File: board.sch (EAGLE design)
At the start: 17 parts, among them J2 632723300011, Q1 16Mhz, U1 MICROCHIP_TECHNOLOGY_MIC5219-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

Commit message: Add reset switch; Minor cleanup
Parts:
- added R6: 10k, rcl:R-EU_R0805
- added S1: (no value), SparkFun-Switches:MOMENTARY-SWITCH-SPST-2-SMD-4.6X2.8MM
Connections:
- new net N$5: R6.2, S1.3, U$1./RESET
- new net N$6: U$1.UVCC
- net GND: now also S1.1
- net VBUS: now also U$1.VBUS
- net VCC: now also R6.1
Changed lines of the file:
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@@
 <part name="C7" library="rcl" library_urn="urn:adsk.eagle:library:334" deviceset="CPOL-EU" device="SMCB" package3d_urn="urn:adsk.eagle:package:25920/5" value="10uF"/>
 <part name="P+2" library="supply1" library_urn="urn:adsk.eagle:library:371" deviceset="VCC" device=""/>
+<part name="P+3" library="supply1" library_urn="urn:adsk.eagle:library:371" deviceset="VCC" device=""/>
+<part name="R6" library="rcl" library_urn="urn:adsk.eagle:library:334" deviceset="R-EU_" device="R0805" package3d_urn="urn:adsk.eagle:package:23553/2" value="10k"/>
+<part name="S1" library="SparkFun-Switches" library_urn="urn:adsk.eagle:library:535" deviceset="MOMENTARY-SWITCH-SPST-2" device="-SMD-4.6X2.8MM" package3d_urn="urn:adsk.eagle:package:40176/1"/>
+<part name="GND10" library="supply1" library_urn="urn:adsk.eagle:library:371" deviceset="GND" device=""/>
 </parts>
 <sheets>
@@
 <segment>
 <pinref part="U1" gate="G$0" pin="IN"/>
-<wire x1="30.48" y1="99.06" x2="22.86" y2="99.06" width="0.1524" layer="91"/>
-<wire x1="22.86" y1="99.06" x2="22.86" y2="83.82" width="0.1524" layer="91"/>
+<wire x1="30.48" y1="99.06" x2="27.94" y2="99.06" width="0.1524" layer="91"/>
+<wire x1="27.94" y1="99.06" x2="27.94" y2="83.82" width="0.1524" layer="91"/>
 <pinref part="U1" gate="G$0" pin="EN"/>
-<wire x1="22.86" y1="83.82" x2="30.48" y2="83.82" width="0.1524" layer="91"/>
-<junction x="22.86" y="99.06"/>
-<label x="7.62" y="99.06" size="1.778" layer="95" rot="R180"/>
-<wire x1="22.86" y1="99.06" x2="15.24" y2="99.06" width="0.1524" layer="91"/>
+<wire x1="27.94" y1="83.82" x2="30.48" y2="83.82" width="0.1524" layer="91"/>
+<junction x="27.94" y="99.06"/>
+<label x="27.94" y="104.14" size="1.778" layer="95" rot="R90" xref="yes"/>
 <pinref part="C7" gate="G$1" pin="+"/>
-<wire x1="15.24" y1="99.06" x2="7.62" y2="99.06" width="0.1524" layer="91"/>
+<wire x1="27.94" y1="99.06" x2="15.24" y2="99.06" width="0.1524" layer="91"/>
 <wire x1="15.24" y1="99.06" x2="15.24" y2="96.52" width="0.1524" layer="91"/>
 <junction x="15.24" y="99.06"/>
+<label x="15.24" y="104.14" size="1.778" layer="95" rot="R90"/>
+<wire x1="15.24" y1="99.06" x2="15.24" y2="104.14" width="0.1524" layer="91"/>
+<wire x1="27.94" y1="104.14" x2="27.94" y2="99.06" width="0.1524" layer="91"/>
+<junction x="27.94" y="99.06"/>
 </segment>
 </net>
@@
 <attribute name="VALUE" x="22.86" y="2.54" size="1.778" layer="96"/>
 </instance>
+<instance part="P+3" gate="VCC" x="2.54" y="83.82" smashed="yes" rot="R90">
+<attribute name="VALUE" x="2.54" y="86.36" size="1.778" layer="96" rot="R180"/>
+</instance>
+<instance part="R6" gate="G$1" x="15.24" y="83.82" smashed="yes">
+<attribute name="NAME" x="11.43" y="85.3186" size="1.778" layer="95"/>
+<attribute name="VALUE" x="11.43" y="80.518" size="1.778" layer="96"/>
+</instance>
+<instance part="S1" gate="G$1" x="15.24" y="91.44" smashed="yes">
+<attribute name="NAME" x="15.24" y="96.266" size="1.778" layer="95" font="vector" align="bottom-center"/>
+<attribute name="VALUE" x="15.24" y="88.646" size="1.778" layer="96" font="vector" align="top-center"/>
+</instance>
+<instance part="GND10" gate="1" x="2.54" y="91.44" smashed="yes" rot="R270">
+<attribute name="VALUE" x="0" y="93.98" size="1.778" layer="96" rot="R270"/>
+</instance>
 </instances>
 <busses>
@@
 <junction x="25.4" y="15.24"/>
 </segment>
+<segment>
+<pinref part="GND10" gate="1" pin="GND"/>
+<pinref part="S1" gate="G$1" pin="1"/>
+<wire x1="5.08" y1="91.44" x2="10.16" y2="91.44" width="0.1524" layer="91"/>
+</segment>
 </net>
 <net name="N$7" class="0">
@@
 </segment>
 </net>
+<net name="VBUS" class="0">
+<segment>
+<pinref part="U$1" gate="G$1" pin="VBUS"/>
+<wire x1="25.4" y1="78.74" x2="20.32" y2="78.74" width="0.1524" layer="91"/>
+<label x="20.32" y="78.74" size="1.27" layer="95" rot="R180" xref="yes"/>
+</segment>
+</net>
+<net name="N$6" class="0">
+<segment>
+<pinref part="U$1" gate="G$1" pin="UVCC"/>
+<wire x1="25.4" y1="66.04" x2="20.32" y2="66.04" width="0.1524" layer="91"/>
+</segment>
+</net>
+<net name="VCC" class="0">
+<segment>
+<pinref part="P+3" gate="VCC" pin="VCC"/>
+<pinref part="R6" gate="G$1" pin="1"/>
+<wire x1="5.08" y1="83.82" x2="10.16" y2="83.82" width="0.1524" layer="91"/>
+</segment>
+</net>
+<net name="N$5" class="0">
+<segment>
+<pinref part="R6" gate="G$1" pin="2"/>
+<pinref part="U$1" gate="G$1" pin="/RESET"/>
+<wire x1="20.32" y1="83.82" x2="25.4" y2="83.82" width="0.1524" layer="91"/>
+<wire x1="25.4" y1="83.82" x2="25.4" y2="91.44" width="0.1524" layer="91"/>
+<junction x="25.4" y="83.82"/>
+<pinref part="S1" gate="G$1" pin="3"/>
+<wire x1="20.32" y1="91.44" x2="25.4" y2="91.44" width="0.1524" layer="91"/>
+</segment>
+</net>

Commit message: Add connections for AtMega32u4
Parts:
- added C10, C8: 1uF, rcl:C-EUC0805
- added C9: 100nF, rcl:C-EUC0805
- added L1: MH2029-300Y, rcl:L-EUL2012C
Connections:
- new net N$8: C9.2, U$1.AREF
- new net N$9: C10.2, L1.1, U$1.AVCC, U$1.AVCC1
- net D+: now also U$1.D+
- net D-: now also U$1.D-
- net GND: now also C10.1, C8.1, C9.1, U$1.UGND
- net N$6: now also C8.2, U$1.UCAP; no longer U$1.UVCC
- net VCC: now also L1.2, U$1.UVCC, U$1.VCC, U$1.VCC1
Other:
- moved on the sheet: C1, C2, Q1

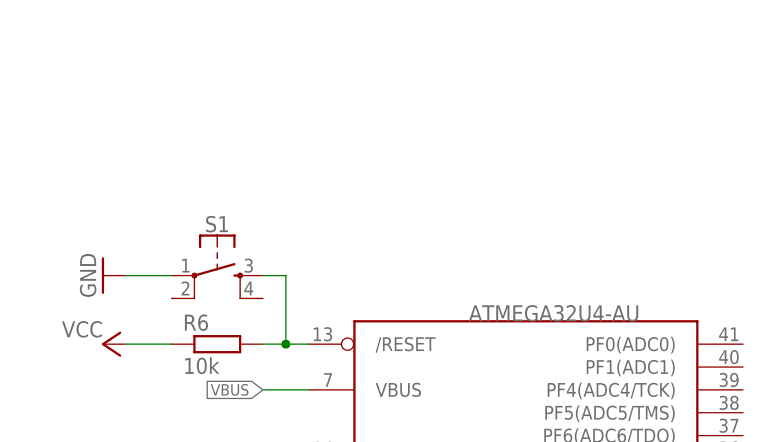
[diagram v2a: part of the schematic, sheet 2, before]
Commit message: Add ISP-6 Header
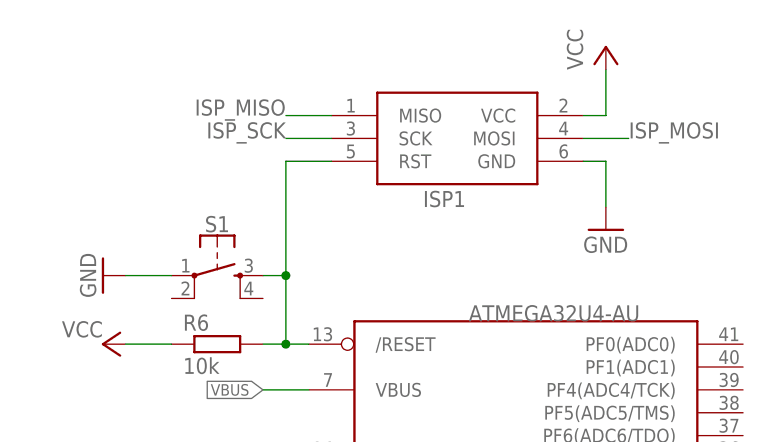
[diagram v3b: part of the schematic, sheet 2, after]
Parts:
- added ISP1: AVRISP-6, adafruit:AVRISP-6
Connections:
- new net ISP_MISO: ISP1.MISO
- new net ISP_MOSI: ISP1.MOSI
- new net ISP_SCK: ISP1.SCK
- net GND: now also ISP1.GND
- net N$5: now also ISP1.RST
- net VCC: now also ISP1.VCC
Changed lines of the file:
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@@
 <part name="GND13" library="supply1" library_urn="urn:adsk.eagle:library:371" deviceset="GND" device=""/>
 <part name="GND14" library="supply1" library_urn="urn:adsk.eagle:library:371" deviceset="GND" device=""/>
+<part name="ISP1" library="adafruit" library_urn="urn:adsk.eagle:library:420" deviceset="AVRISP" device="-6" package3d_urn="urn:adsk.eagle:package:6240744/1"/>
+<part name="P+5" library="supply1" library_urn="urn:adsk.eagle:library:371" deviceset="VCC" device=""/>
+<part name="GND15" library="supply1" library_urn="urn:adsk.eagle:library:371" deviceset="GND" device=""/>
 </parts>
 <sheets>
@@
 <instance part="GND14" gate="1" x="-5.08" y="48.26" smashed="yes" rot="R270">
 <attribute name="VALUE" x="-7.62" y="50.8" size="1.778" layer="96" rot="R270"/>
+</instance>
+<instance part="ISP1" gate="G$1" x="40.64" y="106.68" smashed="yes">
+<attribute name="NAME" x="38.1" y="99.06" size="1.778" layer="95"/>
+</instance>
+<instance part="P+5" gate="VCC" x="58.42" y="116.84" smashed="yes">
+<attribute name="VALUE" x="55.88" y="114.3" size="1.778" layer="96" rot="R90"/>
+</instance>
+<instance part="GND15" gate="1" x="58.42" y="96.52" smashed="yes">
+<attribute name="VALUE" x="55.88" y="93.98" size="1.778" layer="96"/>
 </instance>
 </instances>
@@
 <wire x1="-2.54" y1="60.96" x2="2.54" y2="60.96" width="0.1524" layer="91"/>
 </segment>
+<segment>
+<pinref part="ISP1" gate="G$1" pin="GND"/>
+<wire x1="55.88" y1="104.14" x2="58.42" y2="104.14" width="0.1524" layer="91"/>
+<wire x1="58.42" y1="104.14" x2="58.42" y2="99.06" width="0.1524" layer="91"/>
+<pinref part="GND15" gate="1" pin="GND"/>
+</segment>
 </net>
 <net name="N$7" class="0">
@@
 <junction x="15.24" y="71.12"/>
 </segment>
+<segment>
+<pinref part="P+5" gate="VCC" pin="VCC"/>
+<wire x1="58.42" y1="114.3" x2="58.42" y2="109.22" width="0.1524" layer="91"/>
+<pinref part="ISP1" gate="G$1" pin="VCC"/>
+<wire x1="58.42" y1="109.22" x2="55.88" y2="109.22" width="0.1524" layer="91"/>
+</segment>
 </net>
 <net name="N$5" class="0">
@@
 <wire x1="22.86" y1="83.82" x2="22.86" y2="91.44" width="0.1524" layer="91"/>
 <junction x="22.86" y="83.82"/>
+<pinref part="ISP1" gate="G$1" pin="RST"/>
+<wire x1="27.94" y1="104.14" x2="22.86" y2="104.14" width="0.1524" layer="91"/>
+<wire x1="22.86" y1="104.14" x2="22.86" y2="91.44" width="0.1524" layer="91"/>
+<junction x="22.86" y="91.44"/>
 </segment>
 </net>
@@
 </segment>
 </net>
+<net name="ISP_SCK" class="0">
+<segment>
+<pinref part="ISP1" gate="G$1" pin="SCK"/>
+<wire x1="27.94" y1="106.68" x2="22.86" y2="106.68" width="0.1524" layer="91"/>
+<label x="22.86" y="106.68" size="1.778" layer="95" rot="R180" align="top-left"/>
+</segment>
+</net>
+<net name="ISP_MISO" class="0">
+<segment>
+<pinref part="ISP1" gate="G$1" pin="MISO"/>
+<wire x1="27.94" y1="109.22" x2="22.86" y2="109.22" width="0.1524" layer="91"/>
+<label x="22.86" y="109.22" size="1.778" layer="95" rot="R180" align="top-left"/>
+</segment>
+</net>
+<net name="ISP_MOSI" class="0">
+<segment>
+<pinref part="ISP1" gate="G$1" pin="MOSI"/>
+<wire x1="55.88" y1="106.68" x2="60.96" y2="106.68" width="0.1524" layer="91"/>
+<label x="60.96" y="106.68" size="1.778" layer="95"/>
+</segment>
+</net>

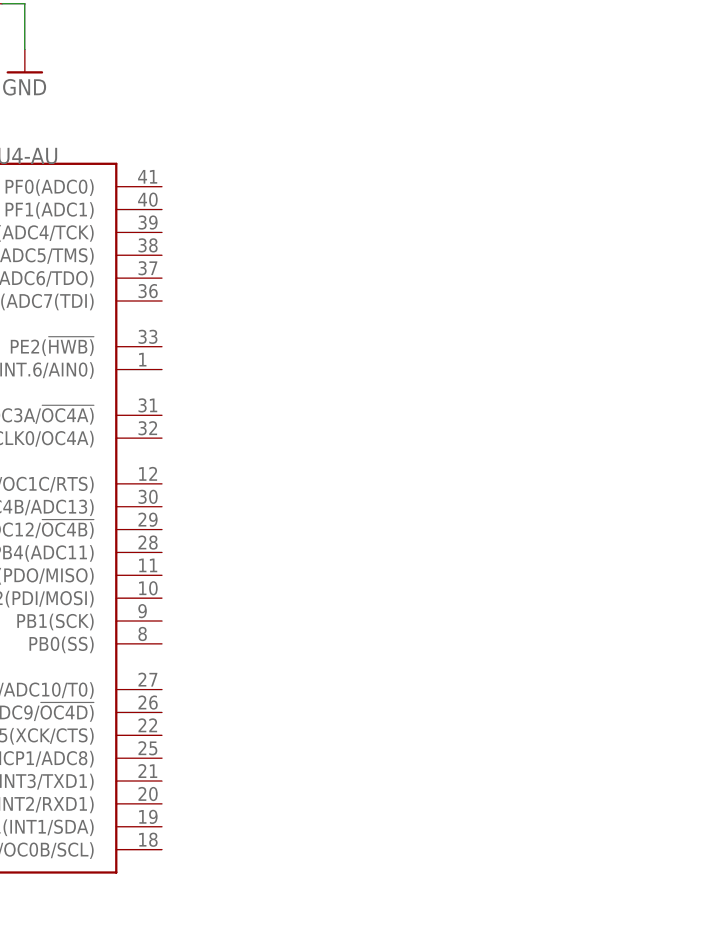
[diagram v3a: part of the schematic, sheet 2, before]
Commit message: Add Analog and Digital IO header
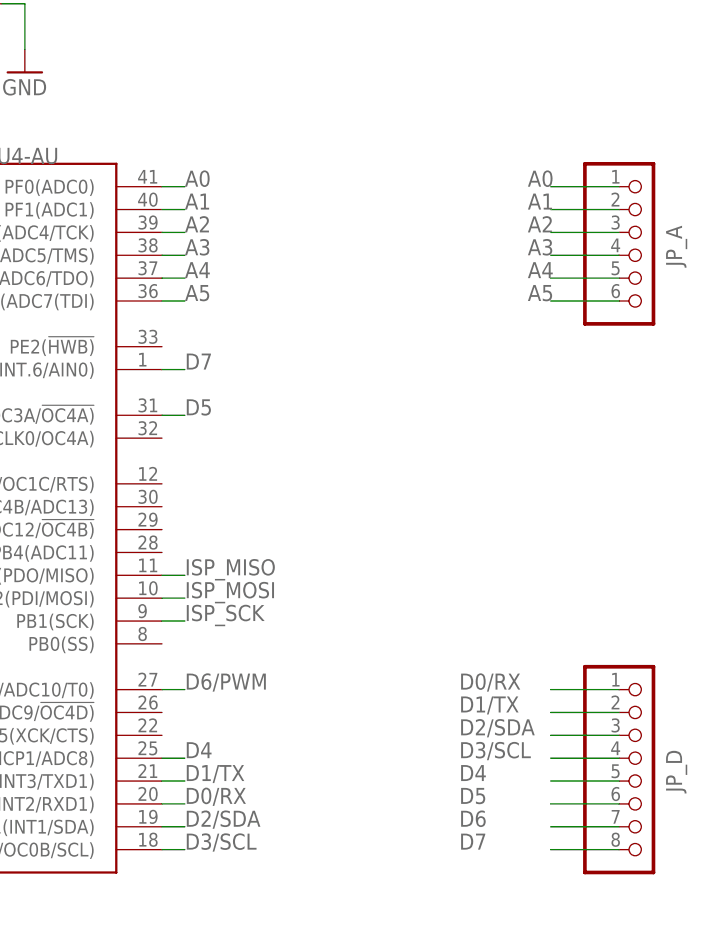
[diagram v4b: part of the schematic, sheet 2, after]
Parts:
- added JP_A: (no value), pinhead:PINHD-1X6
- added JP_D: (no value), pinhead:PINHD-1X8
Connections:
- new net A0: JP_A.1, U$1.PF0(ADC0)
- new net A1: JP_A.2, U$1.PF1(ADC1)
- new net A2: JP_A.3, U$1.PF4(ADC4/TCK)
- new net A3: JP_A.4, U$1.PF5(ADC5/TMS)
- new net A4: JP_A.5, U$1.PF6(ADC6/TDO)
- new net A5: JP_A.6, U$1.PF7(ADC7(TDI)
- new net D0/RX: JP_D.1, U$1.PD2(INT2/RXD1)
- new net D1/TX: JP_D.2, U$1.PD3(INT3/TXD1)
- new net D2/SDA: JP_D.3, U$1.PD1(INT1/SDA)
- new net D3/SCL: JP_D.4, U$1.PD0(INT0/OC0B/SCL)
- new net D4: JP_D.5, U$1.PD4(ICP1/ADC8)
- new net D5: JP_D.6, U$1.PC6(OC3A/!OC4A)
- new net D6: JP_D.7
- new net D6/PWM: U$1.PD7(OC4D/ADC10/T0)
- new net D7: JP_D.8, U$1.PE6(INT.6/AIN0)
- net ISP_MISO: now also U$1.PB3(PDO/MISO)
- net ISP_MOSI: now also U$1.PB2(PDI/MOSI)
- net ISP_SCK: now also U$1.PB1(SCK)
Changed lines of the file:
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@@
 <part name="P+5" library="supply1" library_urn="urn:adsk.eagle:library:371" deviceset="VCC" device=""/>
 <part name="GND15" library="supply1" library_urn="urn:adsk.eagle:library:371" deviceset="GND" device=""/>
+<part name="JP_A" library="pinhead" library_urn="urn:adsk.eagle:library:325" deviceset="PINHD-1X6" device="" package3d_urn="urn:adsk.eagle:package:22472/2"/>
+<part name="JP_D" library="pinhead" library_urn="urn:adsk.eagle:library:325" deviceset="PINHD-1X8" device="" package3d_urn="urn:adsk.eagle:package:22409/2"/>
 </parts>
 <sheets>
@@
 <instance part="GND15" gate="1" x="58.42" y="96.52" smashed="yes">
 <attribute name="VALUE" x="55.88" y="93.98" size="1.778" layer="96"/>
+</instance>
+<instance part="JP_A" gate="A" x="127" y="76.2" smashed="yes">
+<attribute name="NAME" x="131.445" y="74.93" size="1.778" layer="95" rot="R90"/>
+<attribute name="VALUE" x="120.65" y="66.04" size="1.778" layer="96"/>
+</instance>
+<instance part="JP_D" gate="A" x="127" y="17.78" smashed="yes">
+<attribute name="NAME" x="131.445" y="16.51" size="1.778" layer="95" rot="R90"/>
+<attribute name="VALUE" x="120.65" y="5.08" size="1.778" layer="96"/>
 </instance>
 </instances>
@@
 <label x="22.86" y="106.68" size="1.778" layer="95" rot="R180" align="top-left"/>
 </segment>
+<segment>
+<pinref part="U$1" gate="G$1" pin="PB1(SCK)"/>
+<wire x1="73.66" y1="35.56" x2="76.2" y2="35.56" width="0.1524" layer="91"/>
+<label x="76.2" y="35.56" size="1.778" layer="95"/>
+</segment>
 </net>
 <net name="ISP_MISO" class="0">
@@
 <label x="22.86" y="109.22" size="1.778" layer="95" rot="R180" align="top-left"/>
 </segment>
+<segment>
+<pinref part="U$1" gate="G$1" pin="PB3(PDO/MISO)"/>
+<wire x1="73.66" y1="40.64" x2="76.2" y2="40.64" width="0.1524" layer="91"/>
+<label x="76.2" y="40.64" size="1.778" layer="95"/>
+</segment>
 </net>
 <net name="ISP_MOSI" class="0">
@@
 <label x="60.96" y="106.68" size="1.778" layer="95"/>
 </segment>
-</net>
+<segment>
+<pinref part="U$1" gate="G$1" pin="PB2(PDI/MOSI)"/>
+<wire x1="73.66" y1="38.1" x2="76.2" y2="38.1" width="0.1524" layer="91"/>
+<label x="76.2" y="38.1" size="1.778" layer="95"/>
+</segment>
+</net>
+<net name="D5" class="0">
+<segment>
+<pinref part="U$1" gate="G$1" pin="PC6(OC3A/!OC4A)"/>
+<wire x1="73.66" y1="58.42" x2="76.2" y2="58.42" width="0.1524" layer="91"/>
+<label x="76.2" y="58.42" size="1.778" layer="95"/>
+</segment>
+<segment>
+<pinref part="JP_D" gate="A" pin="6"/>
+<wire x1="124.46" y1="15.24" x2="116.84" y2="15.24" width="0.1524" layer="91"/>
+<label x="106.68" y="15.24" size="1.778" layer="95"/>
+</segment>
+</net>
+<net name="D0/RX" class="0">
+<segment>
+<pinref part="U$1" gate="G$1" pin="PD2(INT2/RXD1)"/>
+<wire x1="73.66" y1="15.24" x2="76.2" y2="15.24" width="0.1524" layer="91"/>
+<label x="76.2" y="15.24" size="1.778" layer="95"/>
+</segment>
+<segment>
+<pinref part="JP_D" gate="A" pin="1"/>
+<wire x1="124.46" y1="27.94" x2="116.84" y2="27.94" width="0.1524" layer="91"/>
+<label x="106.68" y="27.94" size="1.778" layer="95"/>
+</segment>
+</net>
+<net name="D1/TX" class="0">
+<segment>
+<pinref part="U$1" gate="G$1" pin="PD3(INT3/TXD1)"/>
+<wire x1="73.66" y1="17.78" x2="76.2" y2="17.78" width="0.1524" layer="91"/>
+<label x="76.2" y="17.78" size="1.778" layer="95"/>
+</segment>
+<segment>
+<pinref part="JP_D" gate="A" pin="2"/>
+<wire x1="124.46" y1="25.4" x2="116.84" y2="25.4" width="0.1524" layer="91"/>
+<label x="106.68" y="25.4" size="1.778" layer="95"/>
+</segment>
+</net>
+<net name="D3/SCL" class="0">
+<segment>
+<pinref part="U$1" gate="G$1" pin="PD0(INT0/OC0B/SCL)"/>
+<wire x1="73.66" y1="10.16" x2="76.2" y2="10.16" width="0.1524" layer="91"/>
+<label x="76.2" y="10.16" size="1.778" layer="95"/>
+</segment>
+<segment>
+<pinref part="JP_D" gate="A" pin="4"/>
+<wire x1="124.46" y1="20.32" x2="116.84" y2="20.32" width="0.1524" layer="91"/>
+<label x="106.68" y="20.32" size="1.778" layer="95"/>
+</segment>
+</net>
+<net name="D4" class="0">
+<segment>
+<pinref part="U$1" gate="G$1" pin="PD4(ICP1/ADC8)"/>
+<wire x1="73.66" y1="20.32" x2="76.2" y2="20.32" width="0.1524" layer="91"/>
+<label x="76.2" y="20.32" size="1.778" layer="95"/>
+</segment>
+<segment>
+<pinref part="JP_D" gate="A" pin="5"/>
+<wire x1="124.46" y1="17.78" x2="116.84" y2="17.78" width="0.1524" layer="91"/>
+<label x="106.68" y="17.78" size="1.778" layer="95"/>
+</segment>
+</net>
+<net name="D2/SDA" class="0">
+<segment>
+<pinref part="U$1" gate="G$1" pin="PD1(INT1/SDA)"/>
+<wire x1="73.66" y1="12.7" x2="76.2" y2="12.7" width="0.1524" layer="91"/>
+<label x="76.2" y="12.7" size="1.778" layer="95"/>
+</segment>
+<segment>
+<pinref part="JP_D" gate="A" pin="3"/>
+<wire x1="124.46" y1="22.86" x2="116.84" y2="22.86" width="0.1524" layer="91"/>
+<label x="106.68" y="22.86" size="1.778" layer="95"/>
+</segment>
+</net>
+<net name="D6/PWM" class="0">
+<segment>
+<pinref part="U$1" gate="G$1" pin="PD7(OC4D/ADC10/T0)"/>
+<wire x1="73.66" y1="27.94" x2="76.2" y2="27.94" width="0.1524" layer="91"/>
+<label x="76.2" y="27.94" size="1.778" layer="95"/>
+</segment>
+</net>
+<net name="D7" class="0">
+<segment>
+<pinref part="U$1" gate="G$1" pin="PE6(INT.6/AIN0)"/>
+<wire x1="73.66" y1="63.5" x2="76.2" y2="63.5" width="0.1524" layer="91"/>
+<label x="76.2" y="63.5" size="1.778" layer="95"/>
+</segment>
+<segment>
+<pinref part="JP_D" gate="A" pin="8"/>
+<wire x1="124.46" y1="10.16" x2="116.84" y2="10.16" width="0.1524" layer="91"/>
+<label x="106.68" y="10.16" size="1.778" layer="95"/>
+</segment>
+</net>
+<net name="D6" class="0">
+<segment>
+<pinref part="JP_D" gate="A" pin="7"/>
+<wire x1="124.46" y1="12.7" x2="116.84" y2="12.7" width="0.1524" layer="91"/>
+<label x="106.68" y="12.7" size="1.778" layer="95"/>
+</segment>
+</net>
+<net name="A0" class="0">
+<segment>
+<pinref part="JP_A" gate="A" pin="1"/>
+<wire x1="124.46" y1="83.82" x2="116.84" y2="83.82" width="0.1524" layer="91"/>
+<label x="114.3" y="83.82" size="1.778" layer="95"/>
+</segment>
+<segment>
+<pinref part="U$1" gate="G$1" pin="PF0(ADC0)"/>
+<wire x1="73.66" y1="83.82" x2="76.2" y2="83.82" width="0.1524" layer="91"/>
+<label x="76.2" y="83.82" size="1.778" layer="95"/>
+</segment>
+</net>
+<net name="A1" class="0">
+<segment>
+<pinref part="JP_A" gate="A" pin="2"/>
+<wire x1="124.46" y1="81.28" x2="116.84" y2="81.28" width="0.1524" layer="91"/>
+<label x="114.3" y="81.28" size="1.778" layer="95"/>
+</segment>
+<segment>
+<pinref part="U$1" gate="G$1" pin="PF1(ADC1)"/>
+<wire x1="73.66" y1="81.28" x2="76.2" y2="81.28" width="0.1524" layer="91"/>
+<label x="76.2" y="81.28" size="1.778" layer="95"/>
+</segment>
+</net>
+<net name="A2" class="0">
+<segment>
+<pinref part="JP_A" gate="A" pin="3"/>
+<wire x1="124.46" y1="78.74" x2="116.84" y2="78.74" width="0.1524" layer="91"/>
+<label x="114.3" y="78.74" size="1.778" layer="95"/>
+</segment>
+<segment>
+<pinref part="U$1" gate="G$1" pin="PF4(ADC4/TCK)"/>
+<wire x1="73.66" y1="78.74" x2="76.2" y2="78.74" width="0.1524" layer="91"/>
+<label x="76.2" y="78.74" size="1.778" layer="95"/>
+</segment>
+</net>
+<net name="A3" class="0">
+<segment>
+<pinref part="JP_A" gate="A" pin="4"/>
+<wire x1="124.46" y1="76.2" x2="116.84" y2="76.2" width="0.1524" layer="91"/>
+<label x="114.3" y="76.2" size="1.778" layer="95"/>
+</segment>
+<segment>
+<pinref part="U$1" gate="G$1" pin="PF5(ADC5/TMS)"/>
+<wire x1="73.66" y1="76.2" x2="76.2" y2="76.2" width="0.1524" layer="91"/>
+<label x="76.2" y="76.2" size="1.778" layer="95"/>
+</segment>
+</net>
+<net name="A4" class="0">
+<segment>
+<pinref part="JP_A" gate="A" pin="5"/>
+<wire x1="124.46" y1="73.66" x2="116.84" y2="73.66" width="0.1524" layer="91"/>
+<label x="114.3" y="73.66" size="1.778" layer="95"/>
+</segment>
+<segment>
+<pinref part="U$1" gate="G$1" pin="PF6(ADC6/TDO)"/>
+<wire x1="73.66" y1="73.66" x2="76.2" y2="73.66" width="0.1524" layer="91"/>
+<label x="76.2" y="73.66" size="1.778" layer="95"/>
+</segment>
+</net>
+<net name="A5" class="0">
+<segment>
+<pinref part="JP_A" gate="A" pin="6"/>
+<wire x1="124.46" y1="71.12" x2="116.84" y2="71.12" width="0.1524" layer="91"/>
+<label x="114.3" y="71.12" size="1.778" layer="95"/>
+</segment>
+<segment>
+<pinref part="U$1" gate="G$1" pin="PF7(ADC7(TDI)"/>
+<wire x1="73.66" y1="71.12" x2="76.2" y2="71.12" width="0.1524" layer="91"/>
+<label x="76.2" y="71.12" size="1.778" layer="95"/>
+</segment>
+</net>
